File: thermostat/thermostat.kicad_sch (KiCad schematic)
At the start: 13 parts, among them J1 Conn_01x16, J2 Conn_01x12, U1 ATSAMD21G18A-A, U2 SPX3819M5-L-3-3, U3 SS-52400-002

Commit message: thermostat: Use A4 for bat voltage detection
This matches what is done in the current sketch / prototypes to avoid
overloading with the display featherwing
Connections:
- net A4: now also R?.1, R?.2
- net D9: no longer R?.1, R?.2
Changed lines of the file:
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@@
     )
   )
-  (global_label "D9" (shape input) (at 262.89 142.24 180) (fields_autoplaced)
+  (global_label "A4" (shape input) (at 262.89 142.24 180) (fields_autoplaced)
     (effects (font (size 1.27 1.27)) (justify right))
-    (property "Intersheet References" "${INTERSHEET_REFS}" (id 0) (at 257.9974 142.1606 0)
+    (property "Intersheet References" "${INTERSHEET_REFS}" (id 0) (at 258.1788 142.1606 0)
       (effects (font (size 1.27 1.27)) (justify right) hide)
     )

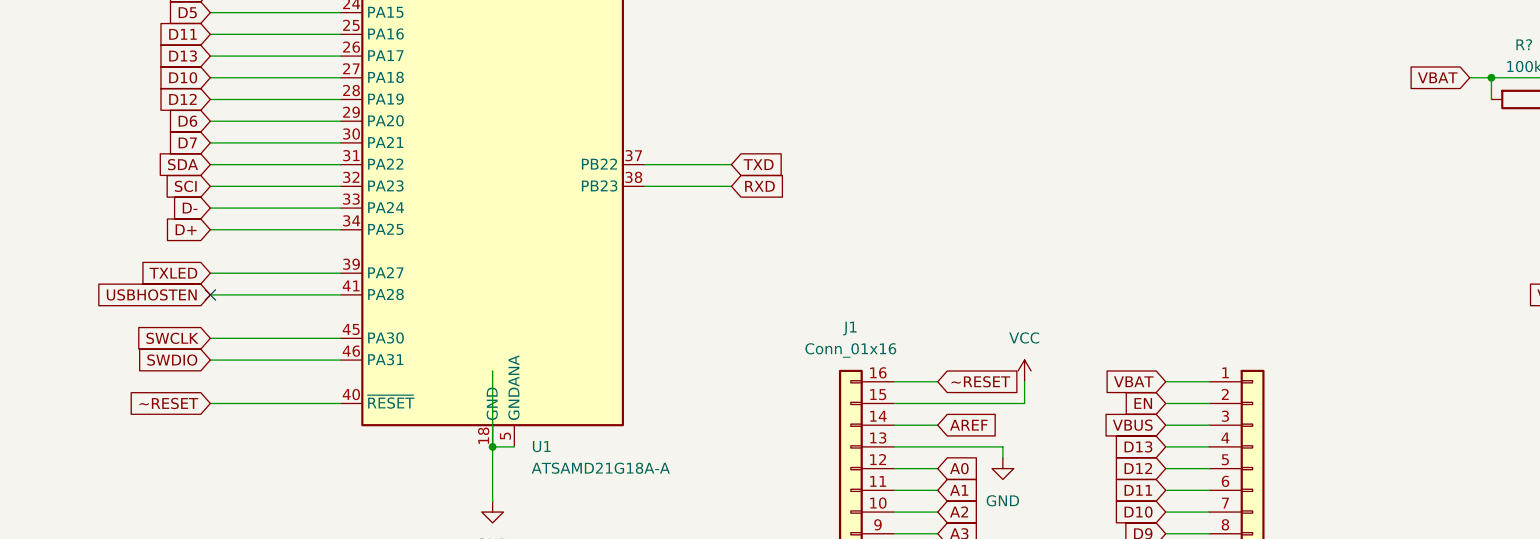
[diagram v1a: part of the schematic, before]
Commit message: thermostat: Add bootstrap programming headers
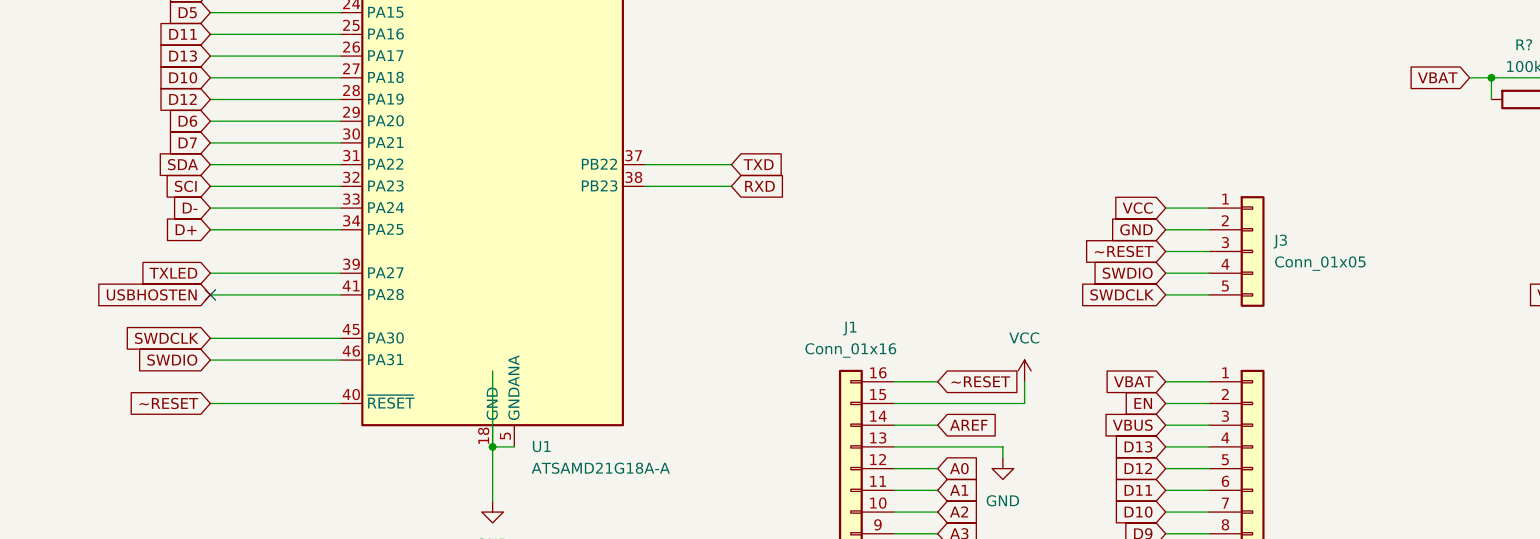
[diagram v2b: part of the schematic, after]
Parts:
- added J3: Conn_01x05, symbol Connector_Generic:Conn_01x05
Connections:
- net GND: now also J3.2 (Pin_2)
- net SWDIO: now also J3.4 (Pin_4)
- net VCC: now also J3.1 (Pin_1)
- net ~RESET: now also J3.3 (Pin_3)
- net SWCLK renamed SWDCLK
- net SWDCLK: now also J3.5 (Pin_5)
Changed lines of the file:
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@@
+    (stroke (width 0) (type default) (color 0 0 0 0))
+  )
+  (wire (pts (xy 168.91 107.95) (xy 173.99 107.95))
     (stroke (width 0) (type default) (color 0 0 0 0))
   )
@@
     (stroke (width 0) (type default) (color 0 0 0 0))
   )
+  (wire (pts (xy 168.91 115.57) (xy 173.99 115.57))
+    (stroke (width 0) (type default) (color 0 0 0 0))
+  )
   (wire (pts (xy 68.58 25.4) (xy 68.58 20.32))
     (stroke (width 0) (type default) (color 0 0 0 0))
@@
     (stroke (width 0) (type default) (color 0 0 0 0))
   )
+  (wire (pts (xy 168.91 113.03) (xy 173.99 113.03))
+    (stroke (width 0) (type default) (color 0 0 0 0))
+  )
   (wire (pts (xy 168.91 125.73) (xy 173.99 125.73))
     (stroke (width 0) (type default) (color 0 0 0 0))
@@
     (stroke (width 0) (type default) (color 0 0 0 0))
   )
+  (wire (pts (xy 168.91 110.49) (xy 173.99 110.49))
+    (stroke (width 0) (type default) (color 0 0 0 0))
+  )
   (wire (pts (xy 97.79 24.13) (xy 97.79 36.83))
     (stroke (width 0) (type default) (color 0 0 0 0))
@@
     (stroke (width 0) (type default) (color 0 0 0 0))
   )
+  (wire (pts (xy 168.91 105.41) (xy 173.99 105.41))
+    (stroke (width 0) (type default) (color 0 0 0 0))
+  )
   (wire (pts (xy 168.91 55.88) (xy 172.72 55.88))
     (stroke (width 0) (type default) (color 0 0 0 0))
@@
     )
   )
-  (global_label "SWCLK" (shape input) (at 57.15 120.65 180) (fields_autoplaced)
-    (effects (font (size 1.27 1.27)) (justify right))
-    (property "Intersheet References" "${INTERSHEET_REFS}" (id 0) (at 48.5079 120.5706 0)
+  (global_label "SWDCLK" (shape input) (at 57.15 120.65 180) (fields_autoplaced)
+    (effects (font (size 1.27 1.27)) (justify right))
+    (property "Intersheet References" "${INTERSHEET_REFS}" (id 0) (at 47.2379 120.5706 0)
       (effects (font (size 1.27 1.27)) (justify right) hide)
     )
@@
     )
   )
+  (global_label "~RESET" (shape input) (at 168.91 110.49 180) (fields_autoplaced)
+    (effects (font (size 1.27 1.27)) (justify right))
+    (property "Intersheet References" "${INTERSHEET_REFS}" (id 0) (at 159.8445 110.4106 0)
+      (effects (font (size 1.27 1.27)) (justify right) hide)
+    )
+  )
   (global_label "A2" (shape input) (at 142.24 140.97 0) (fields_autoplaced)
     (effects (font (size 1.27 1.27)) (justify left))
@@
     )
   )
+  (global_label "GND" (shape input) (at 168.91 107.95 180) (fields_autoplaced)
+    (effects (font (size 1.27 1.27)) (justify right))
+    (property "Intersheet References" "${INTERSHEET_REFS}" (id 0) (at 162.6264 107.8706 0)
+      (effects (font (size 1.27 1.27)) (justify right) hide)
+    )
+  )
   (global_label "D1" (shape input) (at 57.15 69.85 180) (fields_autoplaced)
     (effects (font (size 1.27 1.27)) (justify right))
@@
     )
   )
+  (global_label "SWDCLK" (shape input) (at 168.91 115.57 180) (fields_autoplaced)
+    (effects (font (size 1.27 1.27)) (justify right))
+    (property "Intersheet References" "${INTERSHEET_REFS}" (id 0) (at 158.9979 115.4906 0)
+      (effects (font (size 1.27 1.27)) (justify right) hide)
+    )
+  )
   (global_label "D+" (shape input) (at 57.15 107.95 180) (fields_autoplaced)
     (effects (font (size 1.27 1.27)) (justify right))
@@
     (property "Intersheet References" "${INTERSHEET_REFS}" (id 0) (at 123.9702 100.2506 0)
       (effects (font (size 1.27 1.27)) (justify left) hide)
+    )
+  )
+  (global_label "SWDIO" (shape input) (at 168.91 113.03 180) (fields_autoplaced)
+    (effects (font (size 1.27 1.27)) (justify right))
+    (property "Intersheet References" "${INTERSHEET_REFS}" (id 0) (at 160.6307 112.9506 0)
+      (effects (font (size 1.27 1.27)) (justify right) hide)
+    )
+  )
+  (global_label "VCC" (shape input) (at 168.91 105.41 180) (fields_autoplaced)
+    (effects (font (size 1.27 1.27)) (justify right))
+    (property "Intersheet References" "${INTERSHEET_REFS}" (id 0) (at 162.8683 105.3306 0)
+      (effects (font (size 1.27 1.27)) (justify right) hide)
     )
   )
@@
     (pin "2")
   )
+  (symbol (lib_id "Connector_Generic:Conn_01x05") (at 179.07 110.49 0) (unit 1)
+    (in_bom yes) (on_board yes) (fields_autoplaced)
+    (property "Reference" "J3" (id 0) (at 181.61 109.2199 0)
+      (effects (font (size 1.27 1.27)) (justify left))
+    )
+    (property "Value" "Conn_01x05" (id 1) (at 181.61 111.7599 0)
+      (effects (font (size 1.27 1.27)) (justify left))
+    )
+    (property "Footprint" "" (id 2) (at 179.07 110.49 0)
+      (effects (font (size 1.27 1.27)) hide)
+    )
+    (property "Datasheet" "~" (id 3) (at 179.07 110.49 0)
+      (effects (font (size 1.27 1.27)) hide)
+    )
+    (pin "1")
+    (pin "2")
+    (pin "3")
+    (pin "4")
+    (pin "5")
+  )
   (symbol (lib_id "Device:R") (at 266.7 135.89 0) (unit 1)
     (in_bom yes) (on_board yes) (fields_autoplaced)
@@
       (reference "J2") (unit 1) (value "Conn_01x12") (footprint "")
     )
+    (path "/de22094c-8628-49c1-b5fe-32a92703a5d1"
+      (reference "J3") (unit 1) (value "Conn_01x05") (footprint "")
+    )
     (path "/434cbdf5-0134-4958-9fe9-79d87482e3d4"

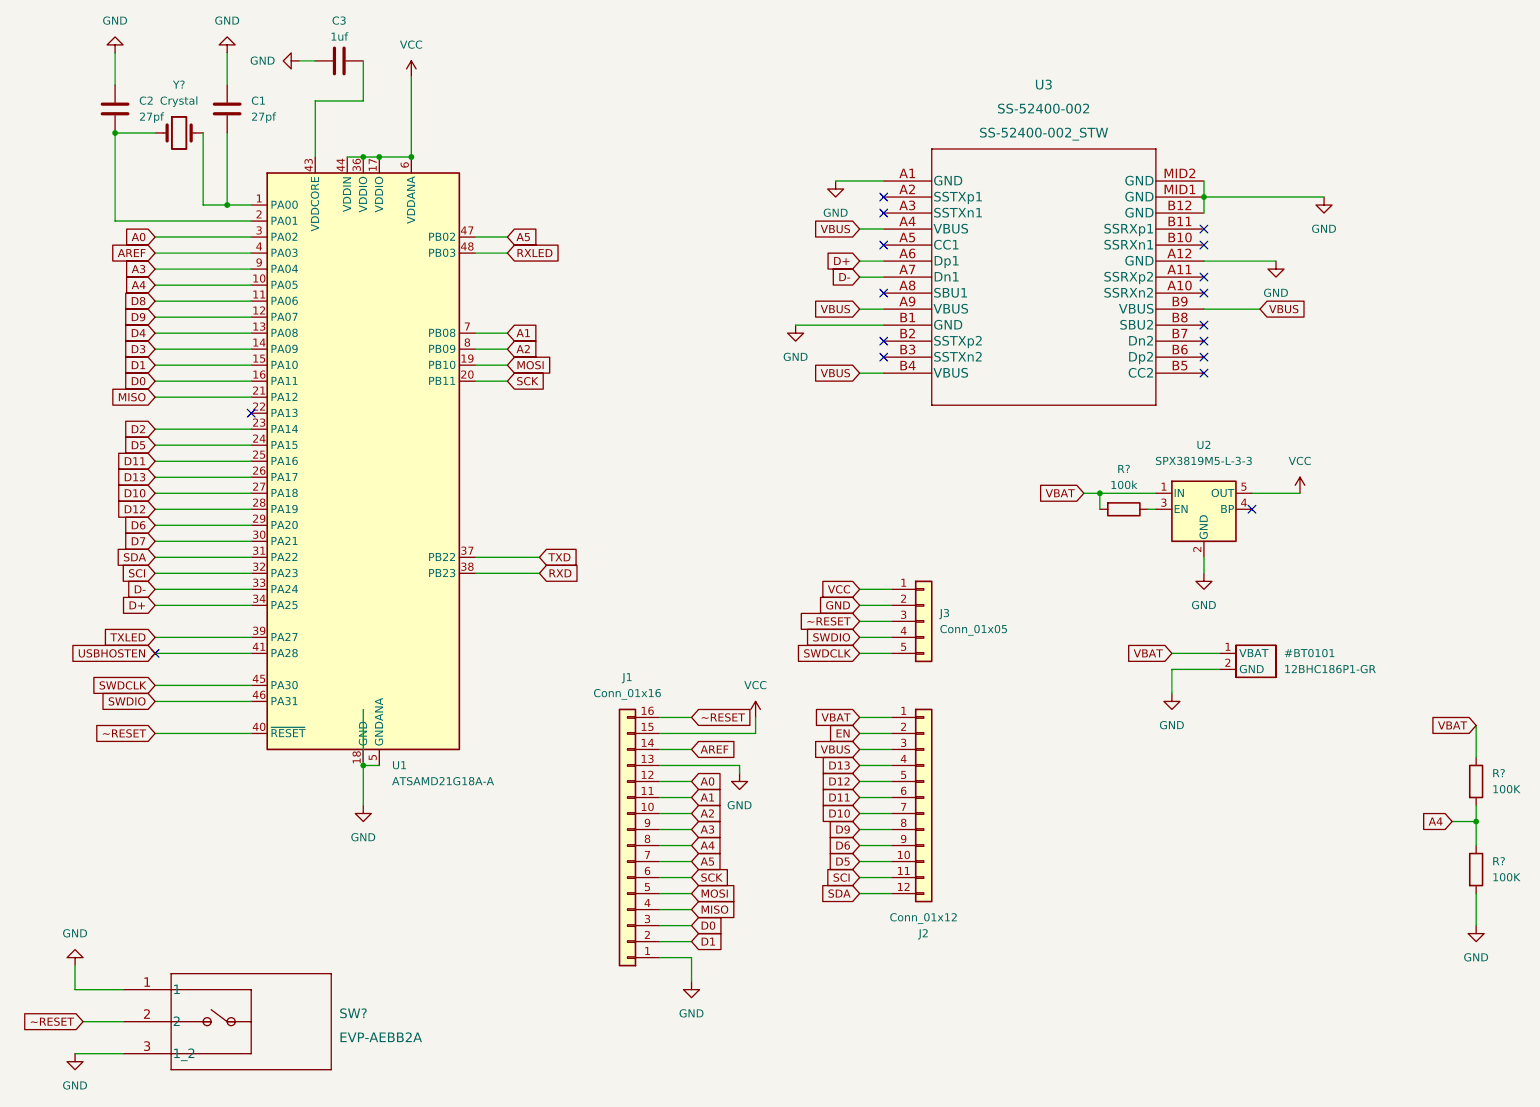
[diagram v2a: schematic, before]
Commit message: thermostat: Connect and label pins
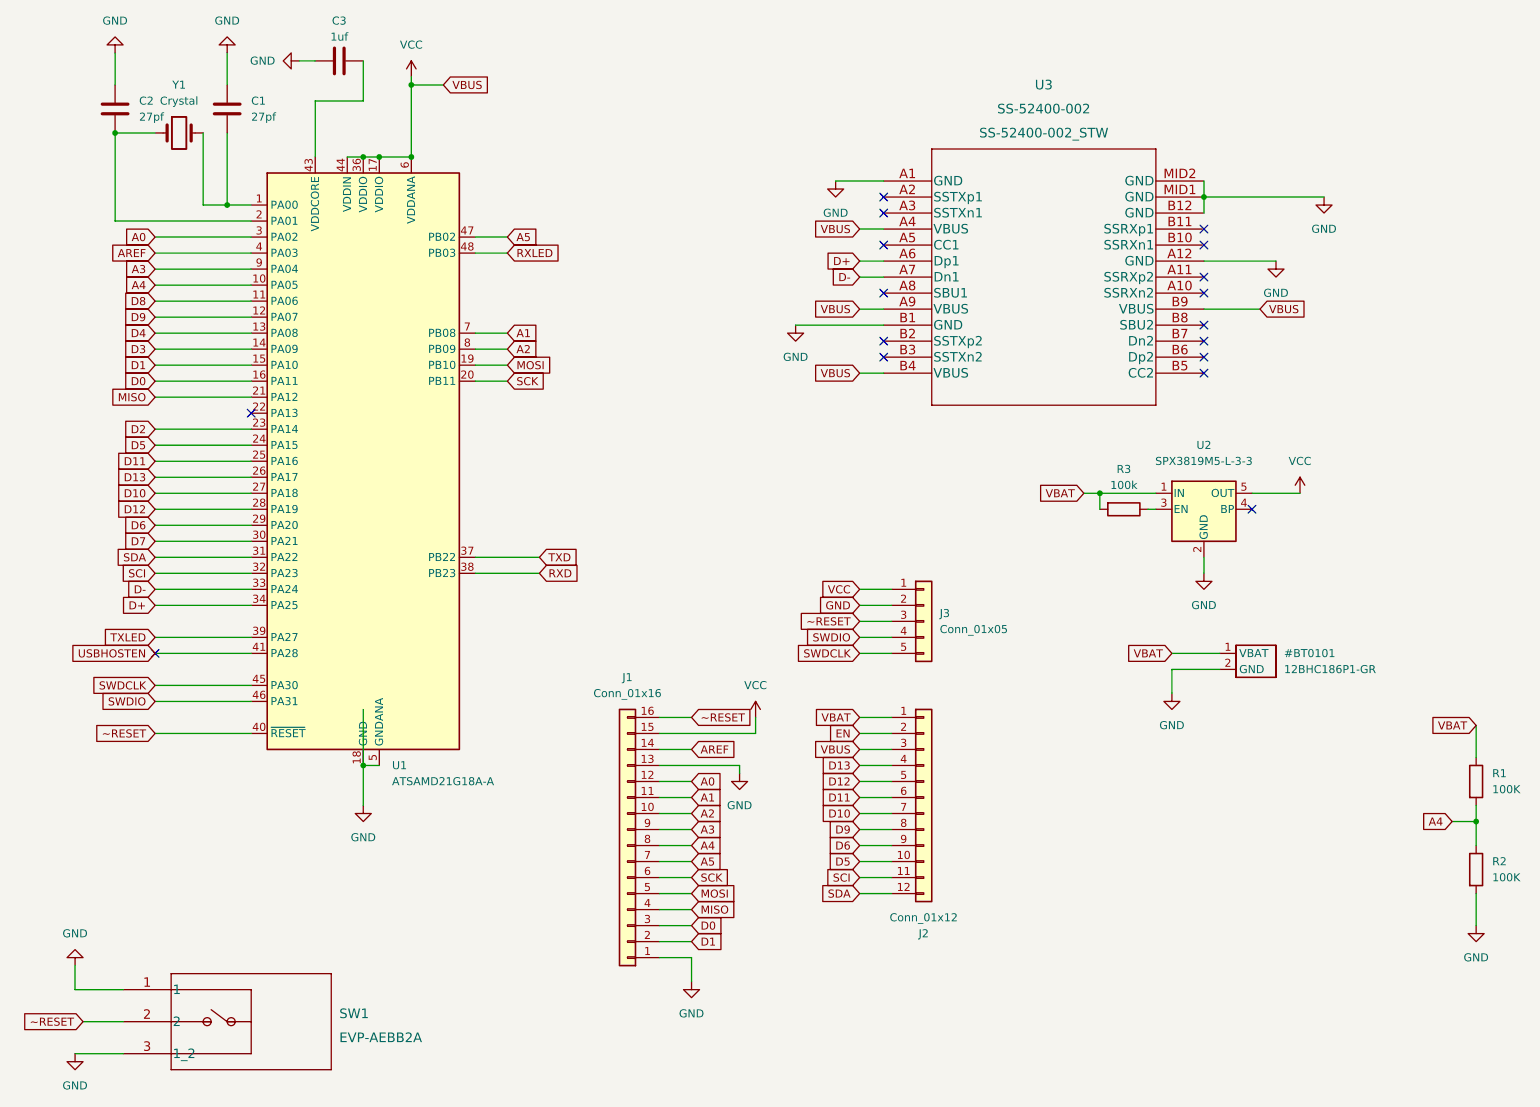
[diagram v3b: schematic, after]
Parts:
- gave numbers to parts that had none: 5
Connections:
- net VBUS is gone; now on net VCC: J2.3 (Pin_3), U3.A4 (VBUS), U3.A9 (VBUS), U3.B4 (VBUS), U3.B9 (VBUS)
